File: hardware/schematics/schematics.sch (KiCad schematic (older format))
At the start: 25 parts, among them J1 Jack-DC, J2 Conn_01x20, J3 Conn_01x20, Q1 Q_NMOS_DGS, U1 ESP32-DevKitC, U2 L7805, U3 MAX6921AUI+

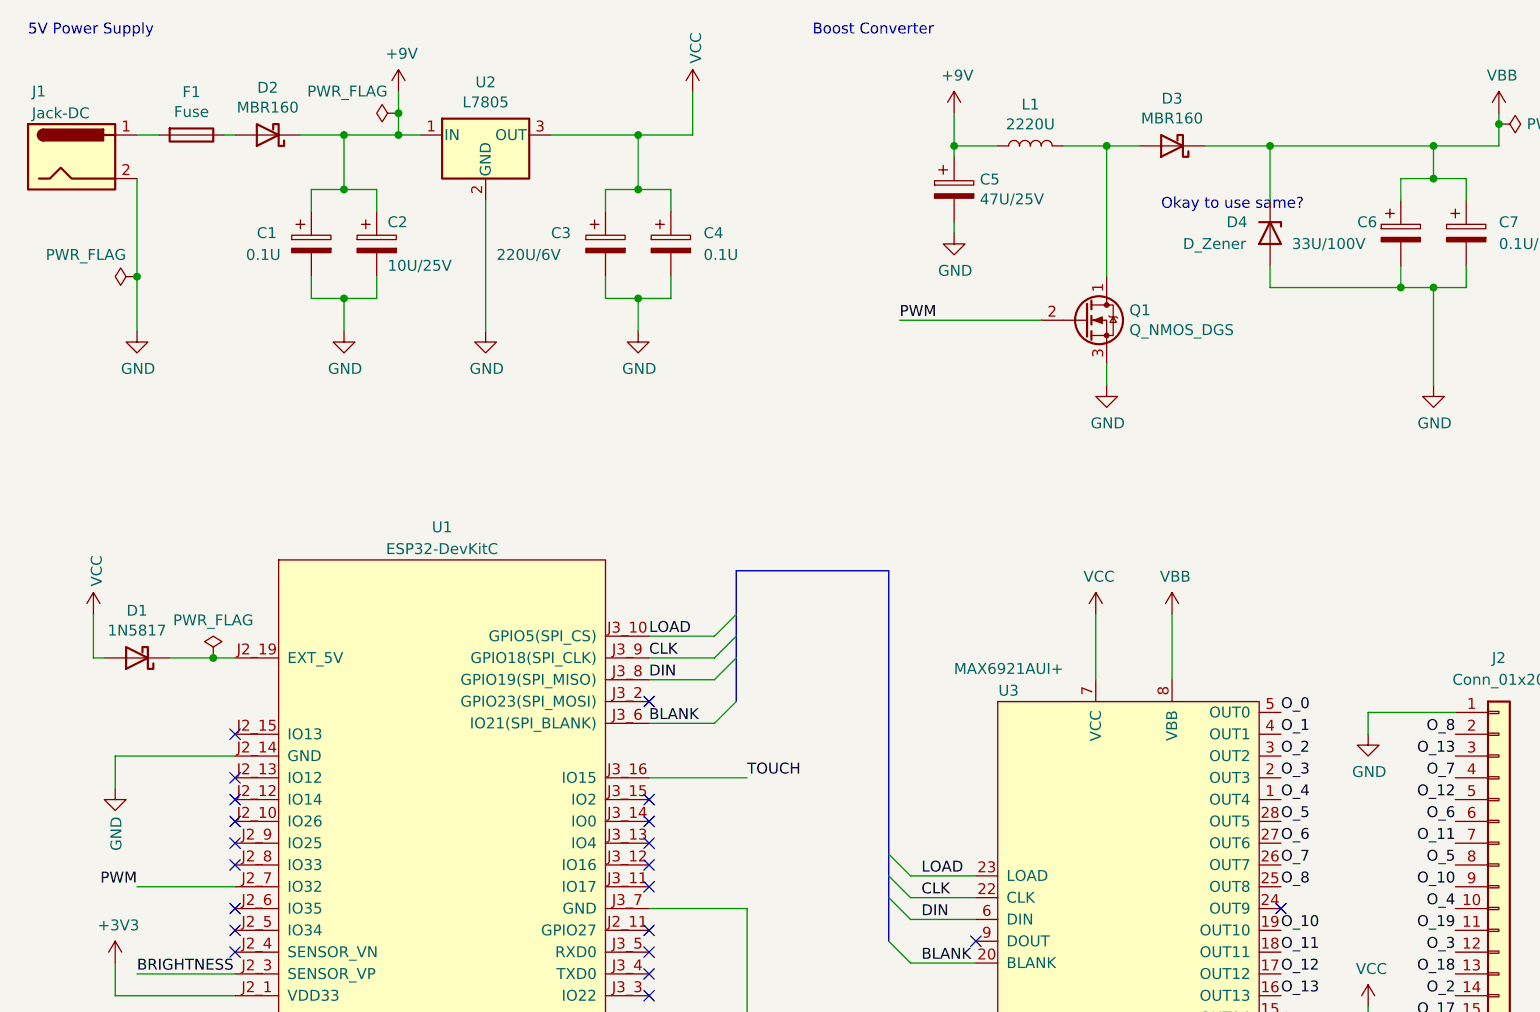
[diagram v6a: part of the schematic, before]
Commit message: Capacitor placements tweaked
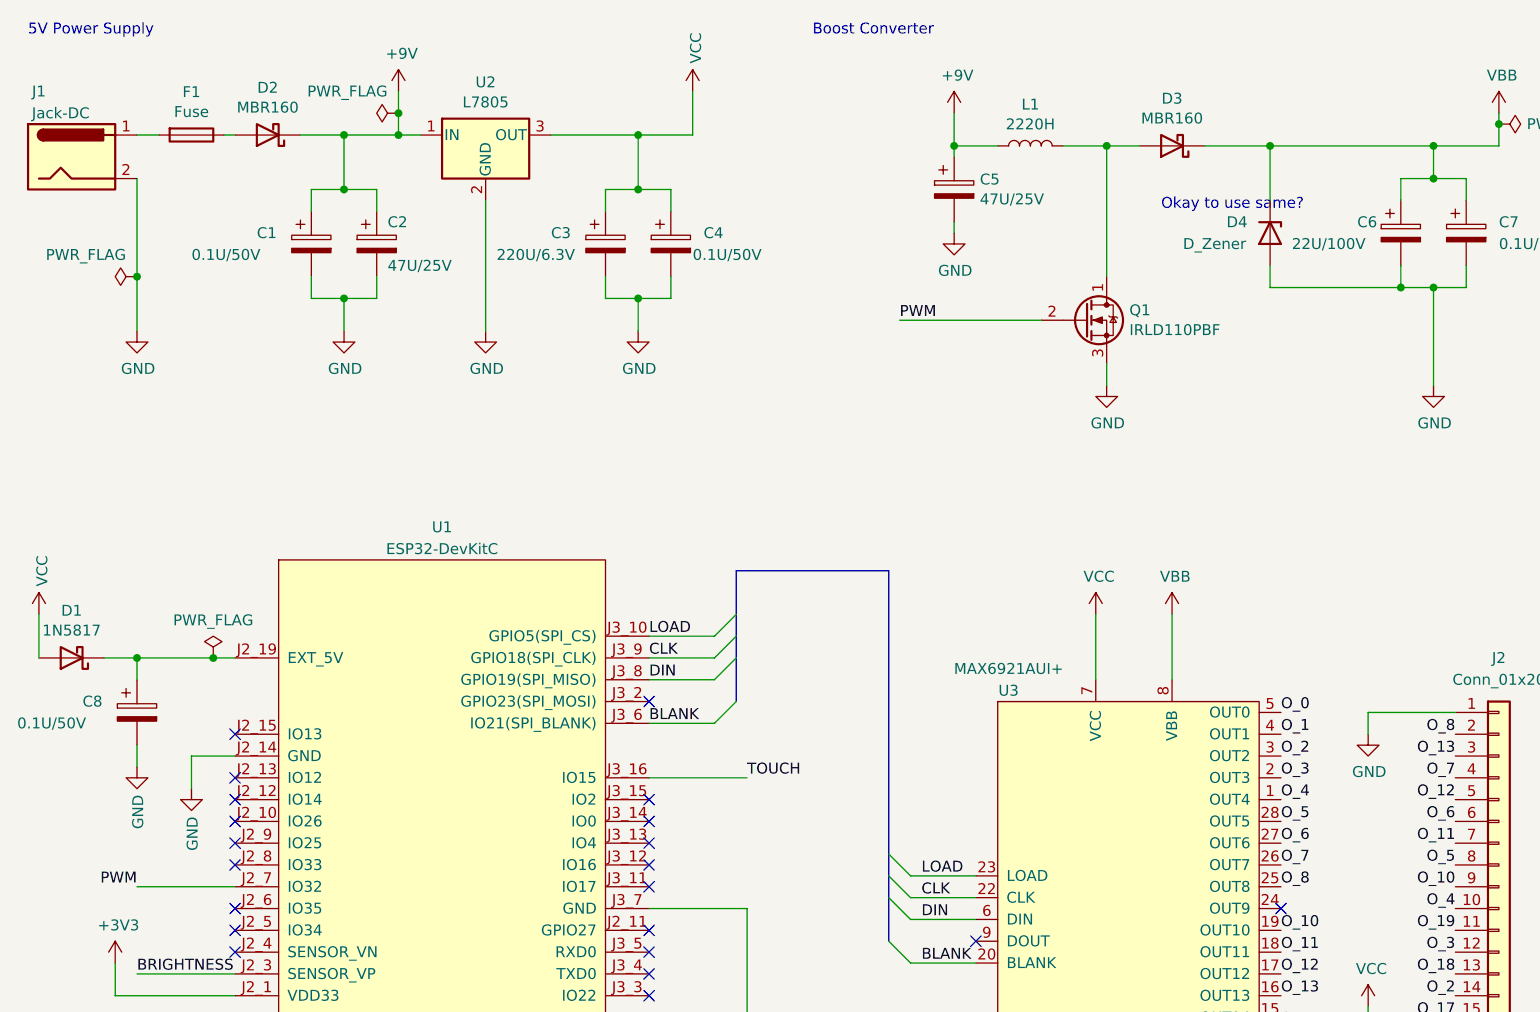
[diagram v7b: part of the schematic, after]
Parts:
- added C8: 0.1U/50V, Capacitor_THT:C_Disc_D3.0mm_W1.6mm_P2.50mm, symbol Device:CP
- C1, C4: value 0.1U -> 0.1U/50V
- C2: value 10U/25V -> 47U/25V
- C3: value 220U/6V -> 220U/6.3V
- C6: value 33U/100V -> 22U/100V
- D1, D2, D3, D4: footprint Diode_THT:D_A-405_P7.62mm_Horizontal -> Diode_THT:D_DO-41_SOD81_P10.16mm_Horizontal
- L1: value 2220U -> 2220H
- Q1: value Q_NMOS_DGS -> IRLD110PBF
- R2, R3: footprint Resistor_THT:R_Axial_DIN0309_L9.0mm_D3.2mm_P12.70mm_Horizontal -> Resistor_THT:R_Axial_DIN0207_L6.3mm_D2.5mm_P10.16mm_Horizontal
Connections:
- net GND: now also C8.2
- net at D1.1 (K), U1.J2_19 (EXT_5V): now also C8.1
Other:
- moved on the sheet: D1
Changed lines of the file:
@@
 P 2000 1700
 F 0 "C1" H 1750 1750 50  0000 L CNN
-F 1 "0.1U" H 1700 1650 50  0000 L CNN
+F 1 " 0.1U/50V" H 1450 1650 50  0000 L CNN
 F 2 "Capacitor_THT:C_Disc_D3.0mm_W1.6mm_P2.50mm" H 2038 1550 50  0001 C CNN
 F 3 "~" H 2000 1700 50  0001 C CNN
@@
 P 2300 1700
 F 0 "C2" H 2350 1800 50  0000 L CNN
-F 1 "10U/25V" H 2350 1600 50  0000 L CNN
+F 1 "47U/25V" H 2350 1600 50  0000 L CNN
 F 2 "Capacitor_THT:CP_Radial_D5.0mm_P2.50mm" H 2338 1550 50  0001 C CNN
 F 3 "~" H 2300 1700 50  0001 C CNN
@@
 L Device:D_Schottky D1
 U 1 1 610DB2FE
-P 1200 3600
-F 0 "D1" H 1200 3383 50  0000 C CNN
-F 1 "1N5817" H 1200 3474 50  0000 C CNN
-F 2 "Diode_THT:D_A-405_P7.62mm_Horizontal" H 1200 3600 50  0001 C CNN
-F 3 "~" H 1200 3600 50  0001 C CNN
-	1    1200 3600
+P 900 3600
+F 0 "D1" H 900 3383 50  0000 C CNN
+F 1 "1N5817" H 900 3474 50  0000 C CNN
+F 2 "Diode_THT:D_DO-41_SOD81_P10.16mm_Horizontal" H 900 3600 50  0001 C CNN
+F 3 "~" H 900 3600 50  0001 C CNN
+	1    900  3600
 	-1   0    0    1
 $EndComp
@@
 P 3350 1700
 F 0 "C3" H 3100 1750 50  0000 L CNN
-F 1 "220U/6V" H 2850 1650 50  0000 L CNN
+F 1 "220U/6.3V" H 2850 1650 50  0000 L CNN
 F 2 "Capacitor_THT:CP_Radial_D6.3mm_P2.50mm" H 3388 1550 50  0001 C CNN
 F 3 "~" H 3350 1700 50  0001 C CNN
@@
 P 5300 1250
 F 0 "L1" V 5490 1250 50  0000 C CNN
-F 1 "2220U" V 5399 1250 50  0000 C CNN
+F 1 "2220H" V 5399 1250 50  0000 C CNN
 F 2 "Inductor_THT:L_Radial_D9.5mm_P5.00mm_Fastron_07HVP" H 5300 1250 50  0001 C CNN
 F 3 "~" H 5300 1250 50  0001 C CNN
@@
 P 5550 2050
 F 0 "Q1" H 5754 2096 50  0000 L CNN
-F 1 "Q_NMOS_DGS" H 5754 2005 50  0000 L CNN
+F 1 "IRLD110PBF" H 5754 2005 50  0000 L CNN
 F 2 "Package_DIP:DIP-4_W7.62mm" H 5750 2150 50  0001 C CNN
 F 3 "~" H 5550 2050 50  0001 C CNN
@@
 P 7000 1650
 F 0 "C6" H 6800 1700 50  0000 L CNN
-F 1 "33U/100V" H 6500 1600 50  0000 L CNN
+F 1 "22U/100V" H 6500 1600 50  0000 L CNN
 F 2 "Capacitor_THT:CP_Radial_D6.3mm_P2.50mm" H 7038 1500 50  0001 C CNN
 F 3 "~" H 7000 1650 50  0001 C CNN
@@
 P 3650 1700
 F 0 "C4" H 3800 1750 50  0000 L CNN
-F 1 "0.1U" H 3800 1650 50  0000 L CNN
+F 1 " 0.1U/50V" H 3750 1650 50  0000 L CNN
 F 2 "Capacitor_THT:C_Disc_D3.0mm_W1.6mm_P2.50mm" H 3688 1550 50  0001 C CNN
 F 3 "~" H 3650 1700 50  0001 C CNN
@@
 F 0 "D4" V 6350 1450 50  0000 L CNN
 F 1 "D_Zener" V 6450 1250 50  0000 L CNN
-F 2 "Diode_THT:D_A-405_P7.62mm_Horizontal" H 6400 1650 50  0001 C CNN
+F 2 "Diode_THT:D_DO-41_SOD81_P10.16mm_Horizontal" H 6400 1650 50  0001 C CNN
 F 3 "~" H 6400 1650 50  0001 C CNN
 	1    6400 1650
@@
 	5650 1250 5800 1250
 $Comp
-L power:GND #PWR021
+L power:GND #PWR022
 U 1 1 610EA4D8
 P 7150 2350
-F 0 "#PWR021" H 7150 2100 50  0001 C CNN
+F 0 "#PWR022" H 7150 2100 50  0001 C CNN
 F 1 "GND" H 7155 2177 50  0000 C CNN
 F 2 "" H 7150 2350 50  0001 C CNN
@@
 F 0 "D3" H 5950 1033 50  0000 C CNN
 F 1 "MBR160" H 5950 1124 50  0000 C CNN
-F 2 "Diode_THT:D_A-405_P7.62mm_Horizontal" H 5950 1250 50  0001 C CNN
+F 2 "Diode_THT:D_DO-41_SOD81_P10.16mm_Horizontal" H 5950 1250 50  0001 C CNN
 F 3 "~" H 5950 1250 50  0001 C CNN
 	1    5950 1250
@@
 $EndComp
 $Comp
-L callisto_lib:VBB #PWR022
+L callisto_lib:VBB #PWR023
 U 1 1 610CFC24
 P 7450 1100
-F 0 "#PWR022" H 7450 950 50  0001 C CNN
+F 0 "#PWR023" H 7450 950 50  0001 C CNN
 F 1 "VBB" H 7465 1273 50  0000 C CNN
 F 2 "" H 7450 1100 50  0001 C CNN
@@
 F 0 "D2" H 1800 983 50  0000 C CNN
 F 1 "MBR160" H 1800 1074 50  0000 C CNN
-F 2 "Diode_THT:D_A-405_P7.62mm_Horizontal" H 1800 1200 50  0001 C CNN
+F 2 "Diode_THT:D_DO-41_SOD81_P10.16mm_Horizontal" H 1800 1200 50  0001 C CNN
 F 3 "~" H 1800 1200 50  0001 C CNN
 	1    1800 1200
@@
 L power:GND #PWR03
 U 1 1 61183A86
-P 1100 4200
-F 0 "#PWR03" H 1100 3950 50  0001 C CNN
-F 1 "GND" V 1105 4072 50  0000 R CNN
-F 2 "" H 1100 4200 50  0001 C CNN
-F 3 "" H 1100 4200 50  0001 C CNN
-	1    1100 4200
+P 1450 4200
+F 0 "#PWR03" H 1450 3950 50  0001 C CNN
+F 1 "GND" V 1455 4072 50  0000 R CNN
+F 2 "" H 1450 4200 50  0001 C CNN
+F 3 "" H 1450 4200 50  0001 C CNN
+	1    1450 4200
 	1    0    0    -1
 $EndComp
@@
 NoConn ~ 2300 5950
 $Comp
-L power:VCC #PWR02
+L power:VCC #PWR01
 U 1 1 611916B7
-P 1000 3400
-F 0 "#PWR02" H 1000 3250 50  0001 C CNN
-F 1 "VCC" V 1015 3528 50  0000 L CNN
-F 2 "" H 1000 3400 50  0001 C CNN
-F 3 "" H 1000 3400 50  0001 C CNN
-	1    1000 3400
-	1    0    0    -1
-$EndComp
-Wire Wire Line
-	1000 3400 1000 3600
-Wire Wire Line
-	1350 3600 1550 3600
-Wire Wire Line
-	1100 4050 1100 4200
+P 750 3400
+F 0 "#PWR01" H 750 3250 50  0001 C CNN
+F 1 "VCC" V 765 3528 50  0000 L CNN
+F 2 "" H 750 3400 50  0001 C CNN
+F 3 "" H 750 3400 50  0001 C CNN
+	1    750  3400
+	1    0    0    -1
+$EndComp
+Wire Wire Line
+	750  3400 750  3600
+Wire Wire Line
+	1450 4050 1450 4200
 Wire Wire Line
 	3550 4750 4000 4750
@@
 F 0 "R2" V 1693 7100 50  0000 C CNN
 F 1 "10K" V 1784 7100 50  0000 C CNN
-F 2 "Resistor_THT:R_Axial_DIN0309_L9.0mm_D3.2mm_P12.70mm_Horizontal" V 1830 7100 50  0001 C CNN
+F 2 "Resistor_THT:R_Axial_DIN0207_L6.3mm_D2.5mm_P10.16mm_Horizontal" V 1830 7100 50  0001 C CNN
 F 3 "~" H 1900 7100 50  0001 C CNN
 	1    1900 7100
@@
 $EndComp
 $Comp
-L power:VCC #PWR019
+L power:VCC #PWR020
 U 1 1 6117890B
 P 6850 5200
-F 0 "#PWR019" H 6850 5050 50  0001 C CNN
+F 0 "#PWR020" H 6850 5050 50  0001 C CNN
 F 1 "VCC" H 6865 5373 50  0000 C CNN
 F 2 "" H 6850 5200 50  0001 C CNN
@@
 	1100 5000 1100 5150
 $Comp
-L power:+3V3 #PWR01
+L power:+3V3 #PWR02
 U 1 1 61240EF7
 P 1050 6900
-F 0 "#PWR01" H 1050 6750 50  0001 C CNN
+F 0 "#PWR02" H 1050 6750 50  0001 C CNN
 F 1 "+3V3" H 1065 7073 50  0000 C CNN
 F 2 "" H 1050 6900 50  0001 C CNN
@@
 F 0 "R3" H 6750 5400 50  0000 C CNN
 F 1 "22" H 6750 5500 50  0000 C CNN
-F 2 "Resistor_THT:R_Axial_DIN0309_L9.0mm_D3.2mm_P12.70mm_Horizontal" V 6780 5450 50  0001 C CNN
+F 2 "Resistor_THT:R_Axial_DIN0207_L6.3mm_D2.5mm_P10.16mm_Horizontal" V 6780 5450 50  0001 C CNN
 F 3 "~" H 6850 5450 50  0001 C CNN
 	1    6850 5450
@@
 	4950 1100 4950 1250
 $Comp
-L power:PWR_FLAG #FLG0101
+L power:PWR_FLAG #FLG03
 U 1 1 616B78DF
 P 2400 1100
-F 0 "#FLG0101" H 2400 1175 50  0001 C CNN
+F 0 "#FLG03" H 2400 1175 50  0001 C CNN
 F 1 "PWR_FLAG" V 2500 1150 50  0000 L CNN
 F 2 "" H 2400 1100 50  0001 C CNN
@@
 	2400 1100 2400 1200
 $Comp
-L power:PWR_FLAG #FLG0102
+L power:PWR_FLAG #FLG01
 U 1 1 616B8964
 P 1200 1850
-F 0 "#FLG0102" H 1200 1925 50  0001 C CNN
+F 0 "#FLG01" H 1200 1925 50  0001 C CNN
 F 1 "PWR_FLAG" V 1300 1900 50  0000 L CNN
 F 2 "" H 1200 1850 50  0001 C CNN
@@
 	1200 1850 1200 2100
 $Comp
-L power:PWR_FLAG #FLG0103
+L power:PWR_FLAG #FLG04
 U 1 1 616C0C03
 P 7450 1150
-F 0 "#FLG0103" H 7450 1225 50  0001 C CNN
+F 0 "#FLG04" H 7450 1225 50  0001 C CNN
 F 1 "PWR_FLAG" V 7450 1278 50  0000 L CNN
 F 2 "" H 7450 1150 50  0001 C CNN
@@
 	3100 1200 3500 1200
 Wire Wire Line
-	1000 3600 1050 3600
-Wire Wire Line
 	7150 1250 7450 1250
 Connection ~ 7450 1150
@@
 	6400 1250 7150 1250
 $Comp
-L power:PWR_FLAG #FLG0104
+L power:PWR_FLAG #FLG02
 U 1 1 6170EB61
 P 1550 3600
-F 0 "#FLG0104" H 1550 3675 50  0001 C CNN
+F 0 "#FLG02" H 1550 3675 50  0001 C CNN
 F 1 "PWR_FLAG" H 1550 3773 50  0000 C CNN
 F 2 "" H 1550 3600 50  0001 C CNN
@@
 	1550 3600 1650 3600
 $Comp
-L power:PWR_FLAG #FLG0105
+L power:PWR_FLAG #FLG05
 U 1 1 617362D5
 P 9000 5100
-F 0 "#FLG0105" H 9000 5175 50  0001 C CNN
+F 0 "#FLG05" H 9000 5175 50  0001 C CNN
 F 1 "PWR_FLAG" H 9000 5273 50  0000 C CNN
 F 2 "" H 9000 5100 50  0001 C CNN
@@
 	1200 5050 1650 5050
 Wire Wire Line
-	1650 4050 1100 4050
+	1650 4050 1450 4050
 Wire Wire Line
 	1650 4650 1200 4650
@@
 NoConn ~ 6450 5350
 $Comp
-L power:GND #PWR020
+L power:GND #PWR021
 U 1 1 6117ABA5
 P 6850 6250
-F 0 "#PWR020" H 6850 6000 50  0001 C CNN
+F 0 "#PWR021" H 6850 6000 50  0001 C CNN
 F 1 "GND" H 6855 6077 50  0000 C CNN
 F 2 "" H 6850 6250 50  0001 C CNN
@@
 dig_2
 $Comp
-L power:GND #PWR0101
+L power:GND #PWR019
 U 1 1 6120D033
 P 6850 3950
-F 0 "#PWR0101" H 6850 3700 50  0001 C CNN
+F 0 "#PWR019" H 6850 3700 50  0001 C CNN
 F 1 "GND" H 6855 3777 50  0000 C CNN
 F 2 "" H 6850 3950 50  0001 C CNN
@@
 fil_g
 NoConn ~ 8000 3950
-Wire Bus Line
-	4650 3200 4650 4900
-Wire Bus Line
-	3950 3200 3950 3800
-Wire Bus Line
-	8900 3500 8900 5000
-Wire Bus Line
-	11000 3500 11000 5500
-Wire Bus Line
-	8450 3500 8450 5650
 Text Label 8050 4850 0    50   ~ 0
 seg_h
@@
 Text Label 8050 4050 0    50   ~ 0
 seg_g
+$Comp
+L Device:CP C8
+U 1 1 6127D88D
+P 1200 3850
+F 0 "C8" H 950 3900 50  0000 L CNN
+F 1 " 0.1U/50V" H 650 3800 50  0000 L CNN
+F 2 "Capacitor_THT:C_Disc_D3.0mm_W1.6mm_P2.50mm" H 1238 3700 50  0001 C CNN
+F 3 "~" H 1200 3850 50  0001 C CNN
+	1    1200 3850
+	1    0    0    -1
+$EndComp
+$Comp
+L power:GND #PWR024
+U 1 1 612AFC63
+P 1200 4100
+F 0 "#PWR024" H 1200 3850 50  0001 C CNN
+F 1 "GND" V 1205 3972 50  0000 R CNN
+F 2 "" H 1200 4100 50  0001 C CNN
+F 3 "" H 1200 4100 50  0001 C CNN
+	1    1200 4100
+	1    0    0    -1
+$EndComp
+Wire Wire Line
+	1050 3600 1200 3600
+Wire Wire Line
+	1200 3600 1200 3700
+Connection ~ 1200 3600
+Wire Wire Line
+	1200 3600 1550 3600
+Wire Wire Line
+	1200 4000 1200 4100
+Wire Bus Line
+	4650 3200 4650 4900
+Wire Bus Line
+	3950 3200 3950 3800
+Wire Bus Line
+	8900 3500 8900 5000
+Wire Bus Line
+	11000 3500 11000 5500
+Wire Bus Line
+	8450 3500 8450 5650
 $EndSCHEMATC

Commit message: PCB finalized
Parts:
- C1, C4, C8: value 0.1U/50V -> 0.1U/50V
- D4: value D_Zener -> 1N5262B
- R1: footprint OptoDevice:R_LDR_5.1x4.3mm_P3.4mm_Vertical -> Connector_PinHeader_2.54mm:PinHeader_1x02_P2.54mm_Vertical
- TP1: footprint Connector_PinSocket_2.54mm:PinSocket_1x01_P2.54mm_Vertical -> Connector_PinHeader_2.54mm:PinHeader_1x01_P2.54mm_Vertical
- U2: footprint Package_TO_SOT_THT:TO-220-3_Horizontal_TabDown -> Package_TO_SOT_THT:TO-220-3_Vertical
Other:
- note removed: "Okay to use same?"
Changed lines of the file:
@@
 P 2000 1700
 F 0 "C1" H 1750 1750 50  0000 L CNN
-F 1 " 0.1U/50V" H 1450 1650 50  0000 L CNN
+F 1 "0.1U/50V" H 1450 1650 50  0000 L CNN
 F 2 "Capacitor_THT:C_Disc_D3.0mm_W1.6mm_P2.50mm" H 2038 1550 50  0001 C CNN
 F 3 "~" H 2000 1700 50  0001 C CNN
@@
 F 0 "U2" H 2800 1442 50  0000 C CNN
 F 1 "L7805" H 2800 1350 50  0000 C CNN
-F 2 "Package_TO_SOT_THT:TO-220-3_Horizontal_TabDown" H 2825 1050 50  0001 L CIN
+F 2 "Package_TO_SOT_THT:TO-220-3_Vertical" H 2825 1050 50  0001 L CIN
 F 3 "http://www.st.com/content/ccc/resource/technical/document/datasheet/41/4f/b3/b0/12/d4/47/88/CD00000444.pdf/files/CD00000444.pdf/jcr:content/translations/en.CD00000444.pdf" H 2800 1150 50  0001 C CNN
 	1    2800 1200
@@
 P 3650 1700
 F 0 "C4" H 3800 1750 50  0000 L CNN
-F 1 " 0.1U/50V" H 3750 1650 50  0000 L CNN
+F 1 "0.1U/50V" H 3750 1650 50  0000 L CNN
 F 2 "Capacitor_THT:C_Disc_D3.0mm_W1.6mm_P2.50mm" H 3688 1550 50  0001 C CNN
 F 3 "~" H 3650 1700 50  0001 C CNN
@@
 P 6400 1650
 F 0 "D4" V 6350 1450 50  0000 L CNN
-F 1 "D_Zener" V 6450 1250 50  0000 L CNN
+F 1 "1N5262B" V 6450 1250 50  0000 L CNN
 F 2 "Diode_THT:D_DO-41_SOD81_P10.16mm_Horizontal" H 6400 1650 50  0001 C CNN
 F 3 "~" H 6400 1650 50  0001 C CNN
@@
 Text Label 4700 2050 0    50   ~ 0
 PWM
-Text Notes 5900 1550 0    50   ~ 0
-Okay to use same?
 $Comp
 L Device:D_Schottky D3
@@
 F 0 "R1" V 1025 7100 50  0000 C CNN
 F 1 "LDR07" V 1116 7100 50  0000 C CNN
-F 2 "OptoDevice:R_LDR_5.1x4.3mm_P3.4mm_Vertical" V 1525 7100 50  0001 C CNN
+F 2 "Connector_PinHeader_2.54mm:PinHeader_1x02_P2.54mm_Vertical" V 1525 7100 50  0001 C CNN
 F 3 "http://www.tme.eu/de/Document/f2e3ad76a925811312d226c31da4cd7e/LDR07.pdf" H 1350 7050 50  0001 C CNN
 	1    1350 7100
@@
 F 0 "TP1" V 3104 7172 50  0000 R CNN
 F 1 "Touchpad" V 3013 7172 50  0000 R CNN
-F 2 "Connector_PinSocket_2.54mm:PinSocket_1x01_P2.54mm_Vertical" H 2950 7550 50  0001 C CNN
+F 2 "Connector_PinHeader_2.54mm:PinHeader_1x01_P2.54mm_Vertical" H 2950 7550 50  0001 C CNN
 F 3 "" H 2950 7550 50  0001 C CNN
 	1    2950 7350
@@
 	10900 5600 11000 5500
 Wire Wire Line
-	10500 5600 10900 5600
+	10500 5600 10800 5600
 NoConn ~ 5050 4900
 Text Label 3550 3500 0    50   ~ 0
@@
 P 1200 3850
 F 0 "C8" H 950 3900 50  0000 L CNN
-F 1 " 0.1U/50V" H 650 3800 50  0000 L CNN
+F 1 "0.1U/50V" H 700 3800 50  0000 L CNN
 F 2 "Capacitor_THT:C_Disc_D3.0mm_W1.6mm_P2.50mm" H 1238 3700 50  0001 C CNN
 F 3 "~" H 1200 3850 50  0001 C CNN
@@
 Wire Wire Line
 	1200 4000 1200 4100
+$Comp
+L power:PWR_FLAG #FLG0101
+U 1 1 6126ED8D
+P 10800 5600
+F 0 "#FLG0101" H 10800 5675 50  0001 C CNN
+F 1 "PWR_FLAG" H 10800 5773 50  0000 C CNN
+F 2 "" H 10800 5600 50  0001 C CNN
+F 3 "~" H 10800 5600 50  0001 C CNN
+	1    10800 5600
+	-1   0    0    1
+$EndComp
+Connection ~ 10800 5600
+Wire Wire Line
+	10800 5600 10900 5600
 Wire Bus Line
 	4650 3200 4650 4900
